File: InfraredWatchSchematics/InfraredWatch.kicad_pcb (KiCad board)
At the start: 2 copper layers, 40 x 40 mm, 5 parts, among them J1 USB_C_Receptacle_USB2.0_16P, U1 STM32WBA54KEUx, U2 TPS3839DBZ, U4 BQ24074RGT

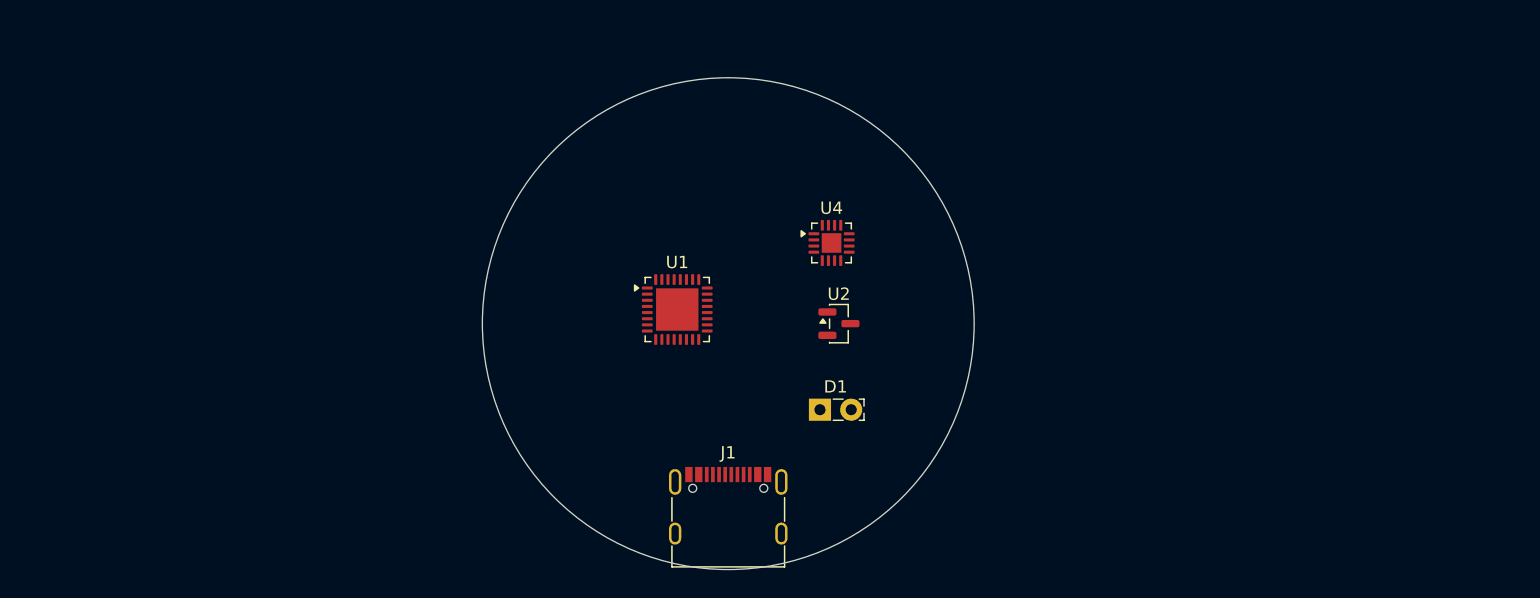
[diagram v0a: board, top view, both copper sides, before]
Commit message: pcb updates, added first watch idea
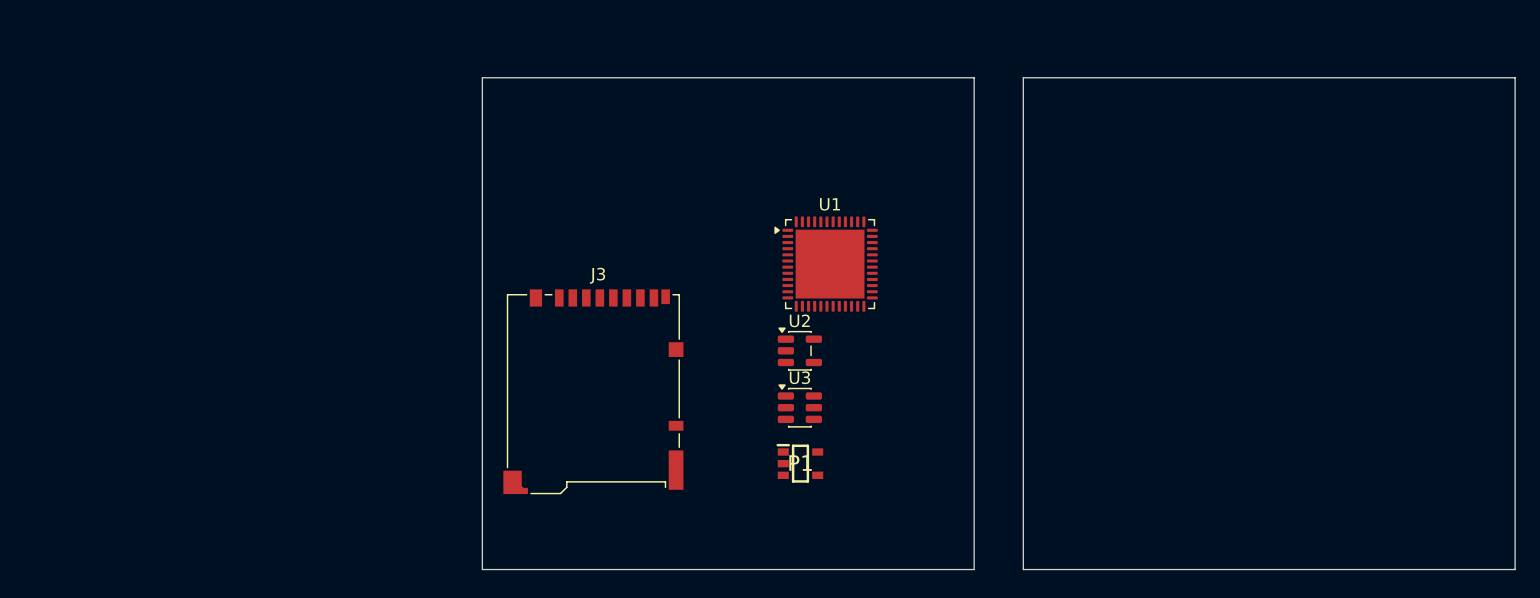
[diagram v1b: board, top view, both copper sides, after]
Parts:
- removed D1: IRL81A, LED_THT:LED_SideEmitter_Rectangular_W4.5mm_H1.6mm
- removed J1: USB_C_Receptacle_USB2.0_16P, Connector_USB:USB_C_Receptacle_G-Switch_GT-USB-7010ASV
- removed U4: BQ24074RGT, Package_DFN_QFN:VQFN-16-1EP_3x3mm_P0.5mm_EP1.6x1.6mm
- added J3: Micro_SD_Card_Det2, Connector_Card:microSD_HC_Hirose_DM3BT-DSF-PEJS, F.Cu at (133.0, 118.5)
- added P1: XC9265A331MR-G, InfraredWatch:XC9265A331MR-G, F.Cu at (149.9, 124.4)
- added U3: USBLC6-2SC6, Package_TO_SOT_SMD:SOT-23-6, F.Cu at (149.8, 119.8)
- U1: value STM32WBA54KEUx -> STM32WB55CGU6; footprint Package_DFN_QFN:QFN-32-1EP_5x5mm_P0.5mm_EP3.45x3.45mm -> Package_DFN_QFN:QFN-48-1EP_7x7mm_P0.5mm_EP5.6x5.6mm
- U2: value TPS3839DBZ -> MCP73831-5-OT; footprint Package_TO_SOT_SMD:SOT-23 -> Package_TO_SOT_SMD:SOT-23-5
- moved U1 13.0 mm to (152.3, 108.2)
- moved U2 3.87 mm to (149.8, 115.2)
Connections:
- U1 pad 1: unconnected-(U1-PB12-Pad1) -> Power
- U1 pad 14: unconnected-(U1-VDD-Pad14) -> /SD_CLK
- U1 pad 15: unconnected-(U1-PB4-Pad15) -> /SD_MISO
- U1 pad 16: unconnected-(U1-PB3-Pad16) -> /SD_MOSI
- U1 pad 2: unconnected-(U1-PA8-Pad2) -> /LSE_In
- U1 pad 20: unconnected-(U1-PA12-Pad20) -> Power
- U1 pad 21: unconnected-(U1-PB15-Pad21) -> /RF
- U1 pad 22: unconnected-(U1-PH3-Pad22) -> GND
- U1 pad 23: unconnected-(U1-VDD-Pad23) -> Power
- U1 pad 24: unconnected-(U1-NRST-Pad24) -> /HSC_Out
- U1 pad 25: unconnected-(U1-RF-Pad25) -> /HSC_In
- U1 pad 3: unconnected-(U1-PA7-Pad3) -> /LSE_Out
- U1 pad 31: unconnected-(U1-VDD-Pad31) -> /SMBSFB
- U1 pad 32: unconnected-(U1-VCAP-Pad32) -> GND
- U1 pad 33: unconnected-(U1-VSS-Pad33) -> /SMBSLX
- U1 pad 4: unconnected-(U1-PA6-Pad4) -> /BOOT0
- U1 pad 8: unconnected-(U1-PA1-Pad8) -> Power
- U2 pad 1: unconnected-(U2-GND-Pad1) -> Net-(D2-K)
- U2 pad 2: unconnected-(U2-~{RESET}-Pad2) -> GND
- U2 pad 3: unconnected-(U2-VDD-Pad3) -> +BATT
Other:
- board size 40 x 40 mm -> 84 x 40 mm

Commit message: Sat Mar 28 22:20:19 EDT 2026
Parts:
- removed J3: Micro_SD_Card_Det2, Connector_Card:microSD_HC_Hirose_DM3BT-DSF-PEJS
- added C1: 4.7uF, Capacitor_SMD:C_0603_1608Metric_Pad1.08x0.95mm_HandSolder, F.Cu at (159.4, 104.7)
- added C10: 4.7uF, Capacitor_SMD:C_0603_1608Metric_Pad1.08x0.95mm_HandSolder, F.Cu at (151.1, 102.0)
- added C11: 10uF, Capacitor_SMD:C_0201_0603Metric_Pad0.64x0.40mm_HandSolder, F.Cu at (182.3, 99.5)
- added C12: 100nF, Capacitor_SMD:C_0402_1005Metric_Pad0.74x0.62mm_HandSolder, F.Cu at (138.3, 105.9)
- added C13: 100nF, Capacitor_SMD:C_0402_1005Metric_Pad0.74x0.62mm_HandSolder, F.Cu at (146.4, 100.5)
- added C14: 22uF, Capacitor_SMD:C_0402_1005Metric_Pad0.74x0.62mm_HandSolder, F.Cu at (185.7, 115.8)
- added C15: C, Capacitor_SMD:C_0402_1005Metric_Pad0.74x0.62mm_HandSolder, F.Cu at (130.4, 100.8)
- added C16: C, Capacitor_SMD:C_0402_1005Metric_Pad0.74x0.62mm_HandSolder, F.Cu at (130.4, 96.4)
- added C17: 4.7uF, Capacitor_SMD:C_0603_1608Metric_Pad1.08x0.95mm_HandSolder, F.Cu at (148.3, 108.9)
- added C18: 0.8pF, Capacitor_SMD:C_0402_1005Metric_Pad0.74x0.62mm_HandSolder, F.Cu at (185.7, 121.7)
- added C19: 0.3pF, Capacitor_SMD:C_0402_1005Metric_Pad0.74x0.62mm_HandSolder, F.Cu at (188.9, 111.8)
- added C2: 4.7uF, Capacitor_SMD:C_0603_1608Metric_Pad1.08x0.95mm_HandSolder, F.Cu at (147.0, 98.6)
- added C20: 100nF, Capacitor_SMD:C_0402_1005Metric_Pad0.74x0.62mm_HandSolder, F.Cu at (188.9, 113.8)
- added C21: 100nF, Capacitor_SMD:C_0402_1005Metric_Pad0.74x0.62mm_HandSolder, F.Cu at (188.9, 115.8)
- added C22: 100nF, Capacitor_SMD:C_0402_1005Metric_Pad0.74x0.62mm_HandSolder, F.Cu at (188.9, 117.7)
- added C23: 100nF, Capacitor_SMD:C_0402_1005Metric_Pad0.74x0.62mm_HandSolder, F.Cu at (188.9, 119.7)
- added C3: 100nF, Capacitor_SMD:C_0402_1005Metric_Pad0.74x0.62mm_HandSolder, F.Cu at (128.1, 96.5)
- added C4: 100nF, Capacitor_SMD:C_0402_1005Metric_Pad0.74x0.62mm_HandSolder, F.Cu at (136.8, 106.0)
- added C5: 100nF, Capacitor_SMD:C_0402_1005Metric_Pad0.74x0.62mm_HandSolder, F.Cu at (143.4, 97.7)
- added C6: 4.7uF, Capacitor_SMD:C_0201_0603Metric_Pad0.64x0.40mm_HandSolder, F.Cu at (157.4, 102.3)
- added C7: 100nF, Capacitor_SMD:C_0402_1005Metric_Pad0.74x0.62mm_HandSolder, F.Cu at (133.2, 94.6)
- added C8: 100nF, Capacitor_SMD:C_0402_1005Metric_Pad0.74x0.62mm_HandSolder, F.Cu at (137.2, 94.7)
- added C9: 100nF, Capacitor_SMD:C_0402_1005Metric_Pad0.74x0.62mm_HandSolder, F.Cu at (128.1, 99.9)
- added D1: CHARGE_INDICATOR, LED_SMD:LED_0402_1005Metric_Pad0.77x0.64mm_HandSolder, F.Cu at (160.0, 96.8)
- added D2: LED, LED_SMD:LED_0402_1005Metric_Pad0.77x0.64mm_HandSolder, F.Cu at (188.0, 125.7)
- added J2: Micro_SD_Card_Det2, Connector_Card:microSD_HC_Hirose_DM3BT-DSF-PEJS, F.Cu at (135.0, 118.6)
- added J4: USB_C_Receptacle_USB2.0_16P, Connector_USB:USB_C_Receptacle_G-Switch_GT-USB-7010ASV, F.Cu at (158.0, 129.0)
- added L1: 10uH, Inductor_SMD:L_0603_1608Metric_Pad1.05x0.95mm_HandSolder, F.Cu at (185.8, 101.4)
- added L2: 10uH, Inductor_SMD:L_0603_1608Metric_Pad1.05x0.95mm_HandSolder, F.Cu at (145.0, 104.5)
- added L3: 10nH, Inductor_SMD:L_0603_1608Metric_Pad1.05x0.95mm_HandSolder, F.Cu at (145.0, 108.0)
- added L4: 2.7nH, Inductor_SMD:L_0603_1608Metric_Pad1.05x0.95mm_HandSolder, F.Cu at (190.2, 96.4)
- added R1: 2k, Resistor_SMD:R_0603_1608Metric_Pad0.98x0.95mm_HandSolder, F.Cu at (162.3, 100.3)
- added R10: 100, Resistor_SMD:R_0201_0603Metric_Pad0.64x0.40mm_HandSolder, F.Cu at (175.0, 99.0)
- added R11: 100, Resistor_SMD:R_0201_0603Metric_Pad0.64x0.40mm_HandSolder, F.Cu at (182.3, 106.5)
- added R12: 100, Resistor_SMD:R_0201_0603Metric_Pad0.64x0.40mm_HandSolder, F.Cu at (182.3, 108.2)
- added R13: 100, Resistor_SMD:R_0201_0603Metric_Pad0.64x0.40mm_HandSolder, F.Cu at (182.3, 110.0)
- added R2: 470, Resistor_SMD:R_0201_0603Metric_Pad0.64x0.40mm_HandSolder, F.Cu at (161.9, 97.6)
- added R3: 5.1k, Resistor_SMD:R_0603_1608Metric_Pad0.98x0.95mm_HandSolder, F.Cu at (190.2, 101.4)
- added R4: 5.1k, Resistor_SMD:R_0603_1608Metric_Pad0.98x0.95mm_HandSolder, F.Cu at (190.2, 103.9)
- added R5: R, Resistor_SMD:R_0603_1608Metric_Pad0.98x0.95mm_HandSolder, F.Cu at (190.2, 106.4)
- added R6: 5.1k, Resistor_SMD:R_0603_1608Metric_Pad0.98x0.95mm_HandSolder, F.Cu at (194.5, 96.4)
- added R7: 5.1k, Resistor_SMD:R_0603_1608Metric_Pad0.98x0.95mm_HandSolder, F.Cu at (194.5, 98.9)
- added R8: 5.1k, Resistor_SMD:R_0603_1608Metric_Pad0.98x0.95mm_HandSolder, F.Cu at (194.5, 101.4)
- added R9: 5.1k, Resistor_SMD:R_0603_1608Metric_Pad0.98x0.95mm_HandSolder, F.Cu at (194.5, 103.9)
- added Y1: 32.768kHz, Crystal:Crystal_SMD_2012-2Pin_2.0x1.2mm_HandSoldering, F.Cu at (130.4, 98.6)
- added Y2: 32MHz, Crystal:Crystal_SMD_SeikoEpson_FA128-4Pin_2.0x1.6mm, F.Cu at (141.3, 105.4)
- U1: value STM32WB55CGU6 -> MCP73831-5-OT; footprint Package_DFN_QFN:QFN-48-1EP_7x7mm_P0.5mm_EP5.6x5.6mm -> Package_TO_SOT_SMD:SOT-23-5
- U2: value MCP73831-5-OT -> USBLC6-2SC6; footprint Package_TO_SOT_SMD:SOT-23-5 -> Package_TO_SOT_SMD:SOT-23-6
- U3: value USBLC6-2SC6 -> STM32WB55CGU6; footprint Package_TO_SOT_SMD:SOT-23-6 -> Package_DFN_QFN:QFN-48-1EP_7x7mm_P0.5mm_EP5.6x5.6mm
- moved P1 33.6 mm to (183.5, 125.0)
- moved U3 24.1 mm to (136.0, 100.1)
- moved U1 10.7 mm to (159.4, 100.2)
- moved U2 8.07 mm to (157.0, 118.9)
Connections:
- U1 pad 1: Power -> Net-(D1-K)
- U1 pad 2: /LSE_In -> GND
- U1 pad 3: /LSE_Out -> +BATT
- U1 pad 4: /BOOT0 -> CHARGE_IN
- U1 pad 5: unconnected-(U1-PB8-Pad5) -> Net-(U1-PROG)
- U2 pad 3: +BATT -> Net-(J4-D+-PadA6)
- U2 pad 4: CHARGE_IN -> /USB_D+
- U2 pad 5: Net-(U2-PROG) -> CHARGE_IN
- U3 pad 1: Net-(J1-D--PadA7) -> Power
- U3 pad 2: GND -> /LSE_In
- U3 pad 3: Net-(J1-D+-PadA6) -> /LSE_Out
- U3 pad 4: /USB_D+ -> /BOOT0/Button3
- U3 pad 5: CHARGE_IN -> unconnected-(U3-PB8-Pad5)
- U3 pad 6: /USB_D- -> unconnected-(U3-PB9-Pad6)
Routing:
- net Power: track 0.00 -> 60.9 mm
- net GND: track 0.00 -> 42.2 mm, vias 0 -> 23
- net CHARGE_IN: track 0.00 -> 38.8 mm
- net /SMBSFB: track 0.00 -> 15.1 mm
- net /SD_MISO: track 0.00 -> 10.3 mm
- net /SD_CLK: track 0.00 -> 8.68 mm
- net /SMBSLX: track 0.00 -> 7.94 mm
- net /LSE_Out: track 0.00 -> 4.16 mm
- net /LSE_In: track 0.00 -> 3.72 mm
- net /HSC_Out: track 0.00 -> 3.49 mm
- net /HSC_In: track 0.00 -> 3.39 mm
- net Net-(D1-K): track 0.00 -> 2.93 mm
- net Net-(U1-PROG): track 0.00 -> 1.82 mm
- net Net-(L2-Pad2): track 0.00 -> 1.72 mm
- net Net-(D1-A): track 0.00 -> 1.50 mm
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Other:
- board size 84 x 40 mm -> 84.1 x 40.3 mm
- copper layers 2 -> 4

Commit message: Sun Mar 29 09:52:52 EDT 2026 added SMD ble chip
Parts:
- added U4: A1001312, InfraredWatch:A1001312, F.Cu at (146.8, 128.2)

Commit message: Wed Apr 29 09:42:28 EDT 2026 | updated pcb
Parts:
- C6: footprint Capacitor_SMD:C_0201_0603Metric_Pad0.64x0.40mm_HandSolder -> Capacitor_SMD:C_0603_1608Metric_Pad1.08x0.95mm_HandSolder
- moved C19 94.5 mm to (94.5, 115.7)
- moved C20 94.5 mm to (94.5, 117.7)
- moved C21 94.5 mm to (94.5, 119.6)
- moved C22 94.5 mm to (94.5, 121.6)
- moved C23 94.5 mm to (94.5, 123.6)
- moved C14 94.5 mm to (91.2, 119.6)
- moved C18 94.5 mm to (91.2, 125.6)
- moved L1 80.6 mm to (105.3, 104.9)
- moved R6 80.5 mm to (114.0, 94.9)
- moved R7 80.5 mm to (114.0, 97.4)
- moved R8 80.5 mm to (114.0, 99.9)
- moved R9 80.5 mm to (114.0, 102.4)
- moved L4 80.5 mm to (109.7, 97.4)
- moved P1 68.3 mm to (115.5, 118.6)
- moved R11 64.9 mm to (117.6, 101.2)
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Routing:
- net Power: track 60.9 -> 0.00 mm
- net GND: track 42.2 -> 0.00 mm, vias 23 -> 0
- net /USB_D+: track 0.00 -> 22.2 mm
- net /USB_D-: track 0.00 -> 19.4 mm
- net CHARGE_IN: track 38.8 -> 23.6 mm, vias 0 -> 2
- net /SMBSFB: track 15.1 -> 0.00 mm
- net Net-(J4-D+-PadA6): track 0.00 -> 12.3 mm
- net Net-(J4-D--PadA7): track 0.00 -> 11.0 mm
- net /SMBSLX: track 7.94 -> 0.00 mm
- net /SD_MOSI: track 0.00 -> 7.64 mm, vias 0 -> 2
- net /IR: track 0.00 -> 7.28 mm, vias 0 -> 2
- net /LSE_Out: track 4.16 -> 0.00 mm
- net /LSE_In: track 3.72 -> 0.00 mm
- net /HSC_Out: track 3.49 -> 0.00 mm
- net /HSC_In: track 3.39 -> 0.00 mm
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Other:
- board size 84.1 x 40.3 mm -> 39.9 x 39.7 mm
